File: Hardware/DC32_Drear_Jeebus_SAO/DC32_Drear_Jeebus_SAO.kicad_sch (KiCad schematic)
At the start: 2 parts, among them J1 Conn_02x03_Top_Bottom

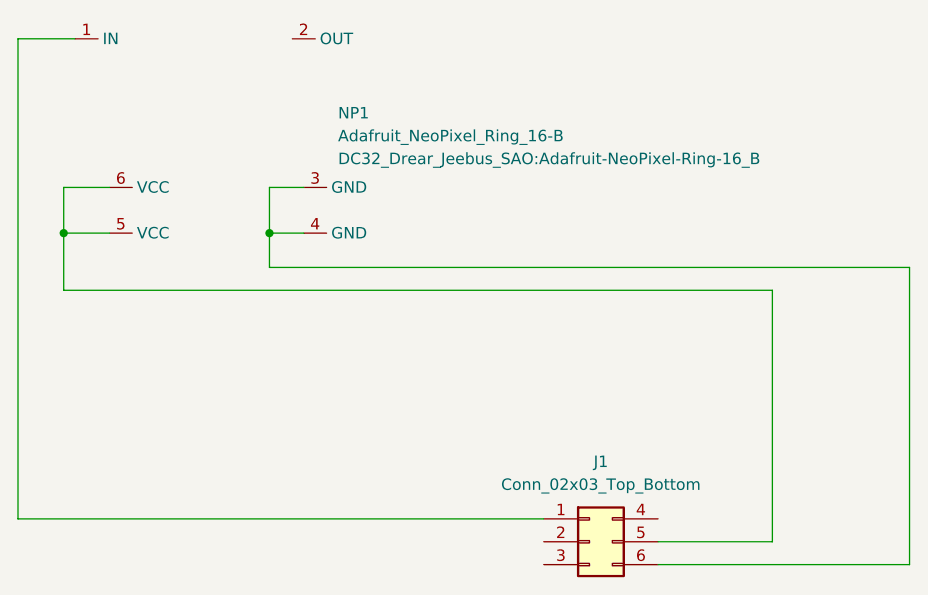
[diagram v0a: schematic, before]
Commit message: Updated schematics and generated PDFs
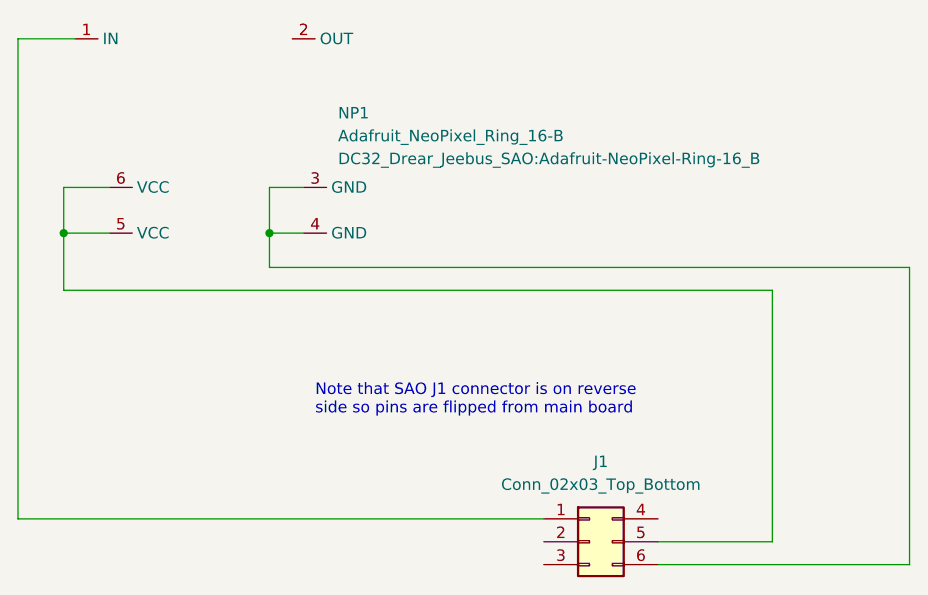
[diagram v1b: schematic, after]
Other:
- note added: "Note that SAO J1 connector is on reverse side so pins are flipped from main board"
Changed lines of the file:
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@@
     (stroke (width 0) (type default))
+  )
+  (text "Note that SAO J1 connector is on reverse\nside so pins are flipped from main board"
+    (at 118.11 104.14 0)
+    (effects (font (size 1.27 1.27)) (justify left bottom))
   )
   (symbol (lib_id "DC32_Drear_Jeebus_SAO:Conn_02x03_Top_Bottom") (at 148.59 118.11 0) (unit 1)
@@
       (effects (font (size 1.27 1.27)) hide)
     )
+    (pin "1")
+    (pin "2")
+    (pin "3")
+    (pin "4")
+    (pin "5")
     (pin "6")
-    (pin "1")
-    (pin "4")
-    (pin "2")
-    (pin "5")
-    (pin "3")
     (instances
       (project "DC32_Drear_Jeebus_SAO"
@@
       (effects (font (size 1.27 1.27)) hide)
     )
-    (pin "4")
-    (pin "6")
     (pin "1")
     (pin "2")
+    (pin "3")
+    (pin "4")
     (pin "5")
-    (pin "3")
+    (pin "6")
     (instances
       (project "DC32_Drear_Jeebus_SAO"
